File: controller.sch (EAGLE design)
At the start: 13 parts, among them IC1 7805DT, J1 POWER_JACKSLT, Q1 MOSFET-NCHANNELBSS123LT1G, Q2 MOSFET-PCHANNELSMD

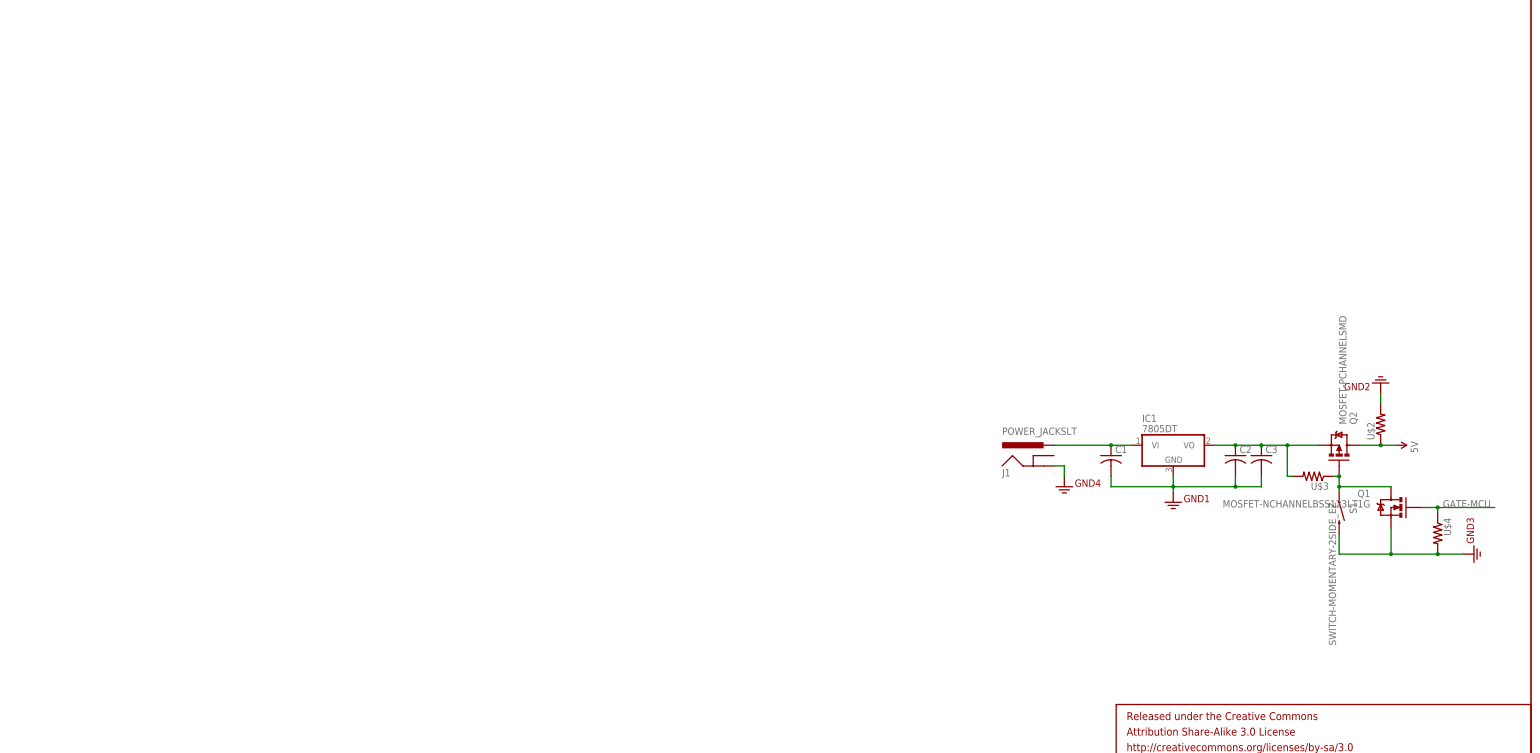
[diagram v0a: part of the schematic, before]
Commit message: removed parts order from repo
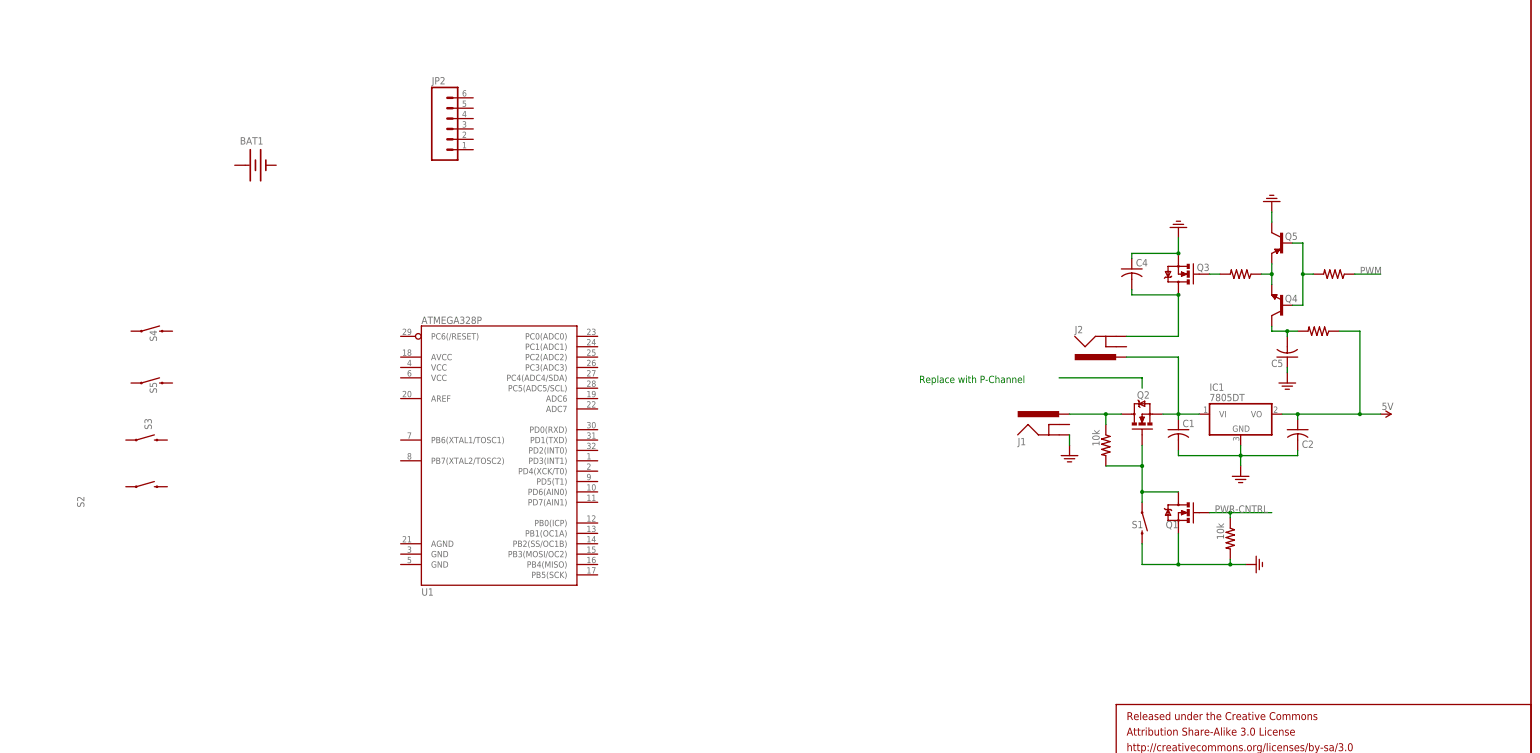
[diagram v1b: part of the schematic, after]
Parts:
- removed C3: (no value), adafruit:C-USC0805
- removed U$2: (no value), jt_parts:RESISTOR
- added BAT1: (no value), SparkFun-Electromechanical:BATTERY12PTH
- added C4, C5: (no value), adafruit:C-USC0805
- added J2: POWER_JACKSLT, SparkFun-Connectors:POWER_JACKSLT
- added JP2: (no value), SparkFun-Connectors:M06SIP
- added Q3: MOSFET-NCHANNELFDD8780, SparkFun-DiscreteSemi:MOSFET-NCHANNELFDD8780
- added Q4: (no value), SparkFun-DiscreteSemi:TRANSISTOR_NPNSOT23
- added Q5: MMBT4403, SparkFun-DiscreteSemi:TRANSISTOR_PNPMMBT4403
- added S2, S3, S4, S5: SWITCH-MOMENTARY-2SIDE_EZ, SparkFun-Electromechanical:SWITCH-MOMENTARY-2SIDE_EZ
- added U$5, U$6, U$7: (no value), jt_parts:RESISTOR
- added U1: ATMEGA328P, SparkFun-DigitalIC:ATMEGA328_SMT
- Q2: value MOSFET-PCHANNELSMD -> MOSFET-NCHANNELFDD8780; device SparkFun-DiscreteSemi:MOSFET-PCHANNELSMD -> SparkFun-DiscreteSemi:MOSFET-NCHANNELFDD8780
- U$3, U$4: value (none) -> 10k
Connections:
- net GATE-MCU renamed PWR-CNTRL
- removed net N$1: C2.1, C3.1, IC1.VO, Q2.S, U$3.2
- new net 12V-IN: J1.PWR, Q2.D, U$3.1
- new net N$10: Q1.D, Q2.G, S1.1, U$3.2
- new net N$3: Q3.G, U$5.2
- new net N$4: C4.2, J2.GND, Q3.D
- new net N$5: Q4.E, Q5.E, U$5.1
- new net NONE: Q4.B, Q5.B, U$6.2
- new net PWM: U$6.1
- net 12V: now also J2.PWR, Q2.S; no longer J1.PWR
- net 5V: now also C2.1, IC1.VO, U$7.1; no longer Q2.D, U$2.1
- net GND: now also C4.1, C5.1, Q3.S, Q5.C; no longer C3.2, U$2.2
- net N$2: now also C5.2, Q4.C, U$7.2; no longer Q1.D, Q2.G, S1.1, U$3.1
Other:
- note added: "Replace with P-Channel"
- moved on the sheet: C1, C2, IC1, J1, Q1, Q2, S1

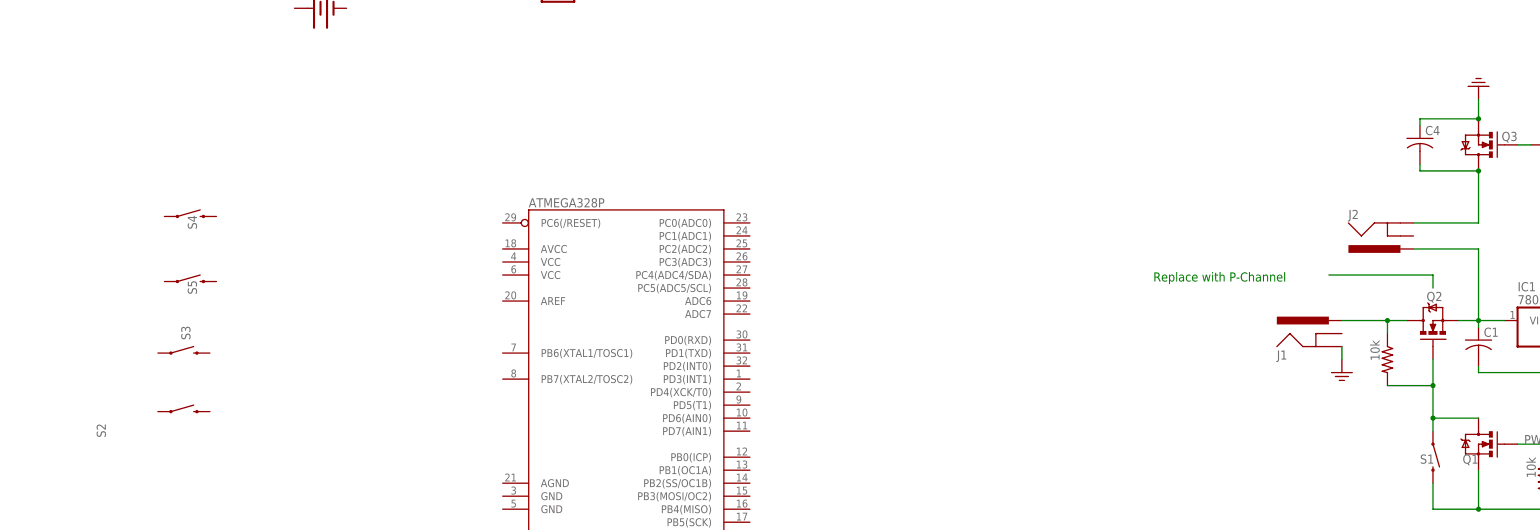
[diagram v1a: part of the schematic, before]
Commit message: reoriented controller to match with display.
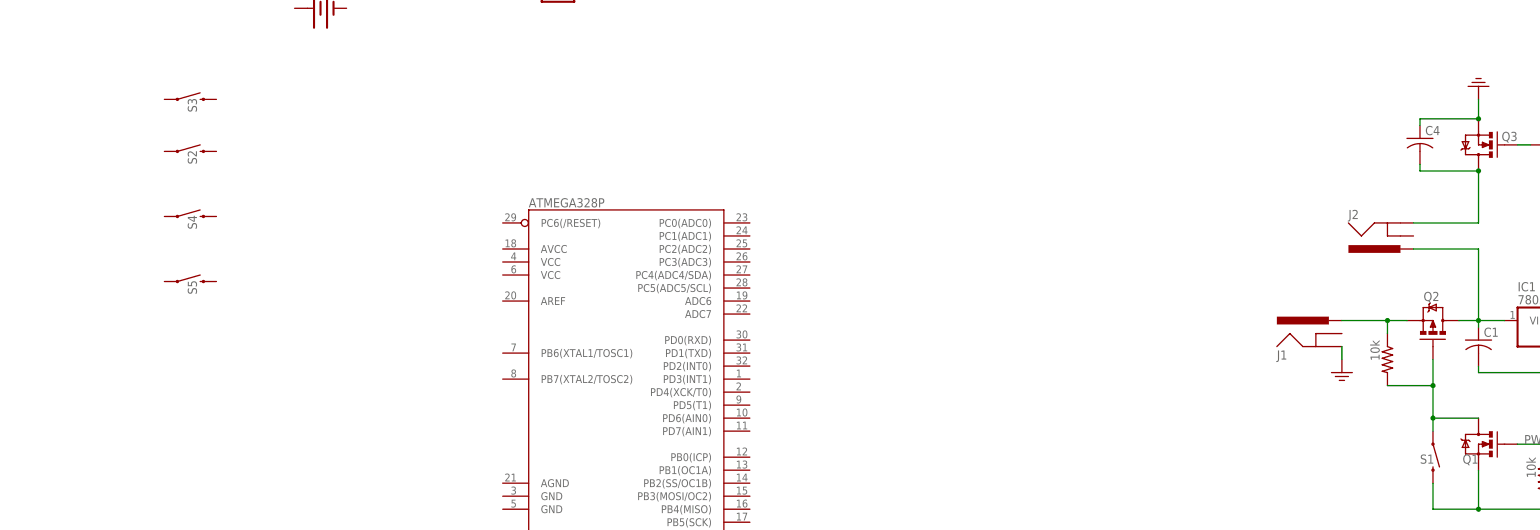
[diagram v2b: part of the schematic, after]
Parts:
- Q2: value MOSFET-NCHANNELFDD8780 -> MOSFET-PCHANNEL; device SparkFun-DiscreteSemi:MOSFET-NCHANNELFDD8780 -> SparkFun-DiscreteSemi:MOSFET-PCHANNEL
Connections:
- net N$4 renamed 12V-RETURN
- net 12V: now also Q2.D; no longer Q2.S
- net 12V-IN: now also Q2.S; no longer Q2.D
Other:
- note removed: "Replace with P-Channel"
- moved on the sheet: S2, S3
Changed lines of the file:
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@@
 <part name="GND5" library="SparkFun-Aesthetics" deviceset="GND2" device=""/>
 <part name="GND6" library="SparkFun-Aesthetics" deviceset="GND2" device=""/>
-<part name="Q2" library="SparkFun-DiscreteSemi" deviceset="MOSFET-NCHANNEL" device="FDD8780"/>
+<part name="Q2" library="SparkFun-DiscreteSemi" deviceset="MOSFET-PCHANNEL" device=""/>
 <part name="U$4" library="jt_parts" deviceset="RESISTOR" device="" value="10k"/>
 <part name="U$6" library="jt_parts" deviceset="RESISTOR" device=""/>
@@
 <part name="BAT1" library="SparkFun-Electromechanical" deviceset="BATTERY" device="12PTH"/>
 <part name="U1" library="SparkFun-DigitalIC" deviceset="ATMEGA328_SMT" device="" value="ATMEGA328P"/>
-<part name="S2" library="SparkFun-Electromechanical" deviceset="SWITCH-MOMENTARY-2" device="SIDE_EZ"/>
-<part name="S3" library="SparkFun-Electromechanical" deviceset="SWITCH-MOMENTARY-2" device="SIDE_EZ"/>
 <part name="S4" library="SparkFun-Electromechanical" deviceset="SWITCH-MOMENTARY-2" device="SIDE_EZ"/>
 <part name="S5" library="SparkFun-Electromechanical" deviceset="SWITCH-MOMENTARY-2" device="SIDE_EZ"/>
 <part name="JP2" library="SparkFun-Connectors" deviceset="M06" device="SIP"/>
+<part name="S2" library="SparkFun-Electromechanical" deviceset="SWITCH-MOMENTARY-2" device="SIDE_EZ"/>
+<part name="S3" library="SparkFun-Electromechanical" deviceset="SWITCH-MOMENTARY-2" device="SIDE_EZ"/>
 </parts>
 <sheets>
 <sheet>
 <plain>
-<text x="274.32" y="124.46" size="1.778" layer="91">Replace with P-Channel</text>
 </plain>
 <instances>
@@
 <instance part="GND5" gate="G$1" x="337.82" y="162.56" smashed="yes" rot="R180"/>
 <instance part="GND6" gate="G$1" x="360.68" y="168.91" smashed="yes" rot="R180"/>
-<instance part="Q2" gate="G$1" x="328.93" y="116.84" smashed="yes" rot="R90">
-<attribute name="NAME" x="327.66" y="120.65" size="1.778" layer="95"/>
+<instance part="Q2" gate="G$1" x="328.93" y="116.84" smashed="yes" rot="MR90">
+<attribute name="NAME" x="330.2" y="120.65" size="1.778" layer="95" rot="MR0"/>
 </instance>
 <instance part="U$4" gate="G$1" x="350.52" y="86.36" smashed="yes" rot="R270">
@@
 <instance part="BAT1" gate="G$1" x="111.76" y="177.8"/>
 <instance part="U1" gate="G$1" x="170.18" y="110.49"/>
-<instance part="S2" gate="G$1" x="85.09" y="99.06" smashed="yes">
-<attribute name="NAME" x="69.85" y="93.98" size="1.778" layer="95" rot="R90"/>
-</instance>
-<instance part="S3" gate="G$1" x="85.09" y="110.49" smashed="yes">
-<attribute name="NAME" x="86.36" y="113.03" size="1.778" layer="95" rot="R90"/>
-</instance>
 <instance part="S4" gate="G$1" x="86.36" y="137.16" smashed="yes">
 <attribute name="NAME" x="87.63" y="134.62" size="1.778" layer="95" rot="R90"/>
@@
 </instance>
 <instance part="JP2" gate="G$1" x="160.02" y="186.69"/>
+<instance part="S2" gate="G$1" x="86.36" y="149.86" smashed="yes">
+<attribute name="NAME" x="87.63" y="147.32" size="1.778" layer="95" rot="R90"/>
+</instance>
+<instance part="S3" gate="G$1" x="86.36" y="160.02" smashed="yes">
+<attribute name="NAME" x="87.63" y="157.48" size="1.778" layer="95" rot="R90"/>
+</instance>
 </instances>
 <busses>
@@
 </segment>
 </net>
-<net name="N$4" class="1">
+<net name="12V-RETURN" class="1">
 <segment>
 <pinref part="J2" gate="G$1" pin="GND"/>
@@
 <net name="N$10" class="0">
 <segment>
-<wire x1="328.93" y1="109.22" x2="328.93" y2="104.14" width="0.1524" layer="91"/>
 <wire x1="328.93" y1="104.14" x2="320.04" y2="104.14" width="0.1524" layer="91"/>
 <pinref part="U$3" gate="G$1" pin="2"/>
@@
 <wire x1="337.82" y1="97.79" x2="328.93" y2="97.79" width="0.1524" layer="91"/>
 <wire x1="328.93" y1="104.14" x2="328.93" y2="97.79" width="0.1524" layer="91"/>
-<junction x="328.93" y="104.14"/>
 <junction x="328.93" y="97.79"/>
 <pinref part="Q2" gate="G$1" pin="G"/>
+<wire x1="328.93" y1="104.14" x2="328.93" y2="109.22" width="0.1524" layer="91"/>
+<junction x="328.93" y="104.14"/>
 </segment>
 </net>
@@
 <pinref part="J2" gate="G$1" pin="PWR"/>
 <wire x1="325.12" y1="130.81" x2="337.82" y2="130.81" width="0.1524" layer="91"/>
-<pinref part="Q2" gate="G$1" pin="S"/>
 <pinref part="IC1" gate="A1" pin="VI"/>
-<wire x1="334.01" y1="116.84" x2="337.82" y2="116.84" width="0.1524" layer="91"/>
 <pinref part="C1" gate="G$1" pin="1"/>
 <wire x1="337.82" y1="116.84" x2="342.9" y2="116.84" width="0.1524" layer="91"/>
@@
 <junction x="337.82" y="116.84"/>
 <wire x1="337.82" y1="130.81" x2="337.82" y2="116.84" width="0.1524" layer="91"/>
-</segment>
-</net>
-<net name="N$1" class="0">
-<segment>
-<wire x1="308.61" y1="125.73" x2="328.93" y2="125.73" width="0.1524" layer="91"/>
-<wire x1="328.93" y1="125.73" x2="328.93" y2="123.19" width="0.1524" layer="91"/>
+<pinref part="Q2" gate="G$1" pin="D"/>
+<wire x1="334.01" y1="116.84" x2="337.82" y2="116.84" width="0.1524" layer="91"/>
 </segment>
 </net>
@@
 <segment>
 <pinref part="J1" gate="G$1" pin="PWR"/>
-<pinref part="Q2" gate="G$1" pin="D"/>
 <wire x1="311.15" y1="116.84" x2="320.04" y2="116.84" width="0.1524" layer="91"/>
 <pinref part="U$3" gate="G$1" pin="1"/>
-<wire x1="320.04" y1="116.84" x2="323.85" y2="116.84" width="0.1524" layer="91"/>
 <wire x1="320.04" y1="114.3" x2="320.04" y2="116.84" width="0.1524" layer="91"/>
+<pinref part="Q2" gate="G$1" pin="S"/>
+<wire x1="323.85" y1="116.84" x2="320.04" y2="116.84" width="0.1524" layer="91"/>
 <junction x="320.04" y="116.84"/>
 </segment>

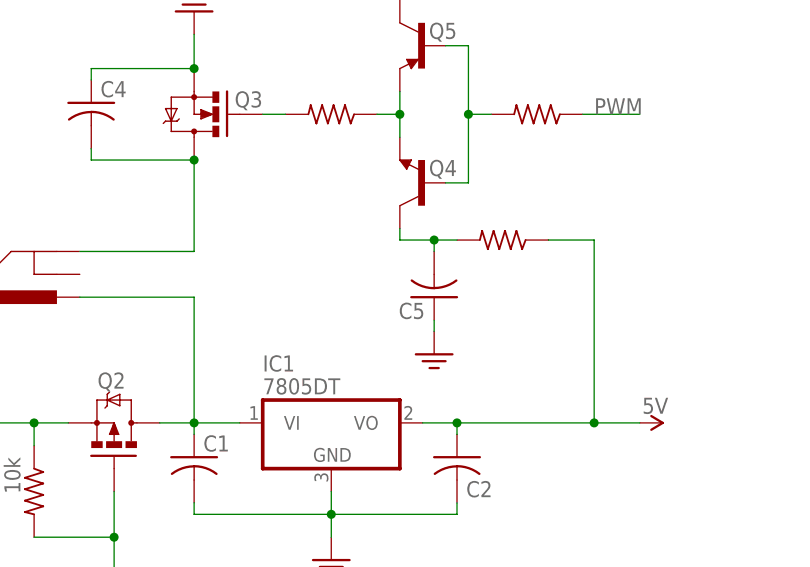
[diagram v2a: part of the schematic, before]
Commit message: fixed inconsistency between board and schematic.
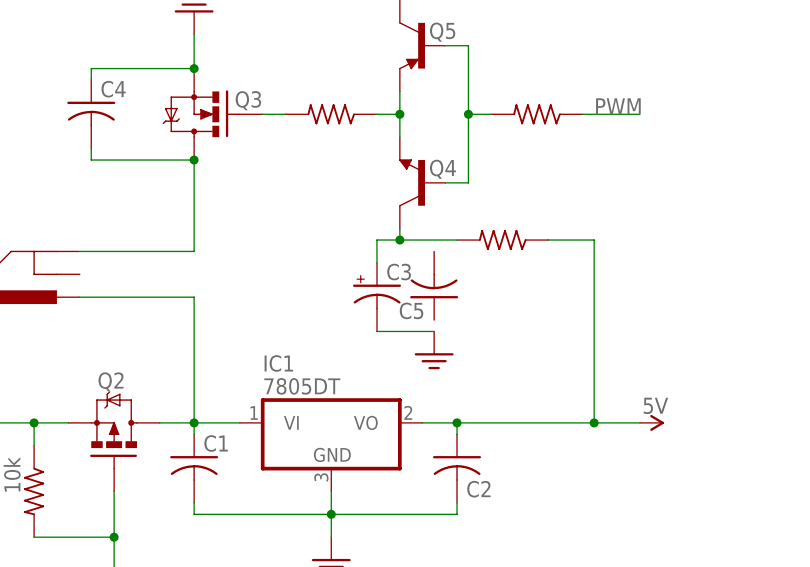
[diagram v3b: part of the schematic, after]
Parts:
- added C3: (no value), adafruit:CPOL-USE22-10AXIAL
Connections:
- new net 3.3V: C3.-
- net GND: no longer C5.1
- net N$2: now also C3.+; no longer C5.2
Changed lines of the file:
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@@
 <setting verticaltext="up"/>
 </settings>
-<grid distance="0.05" unitdist="inch" unit="inch" style="lines" multiple="1" display="yes" altdistance="0.01" altunitdist="inch" altunit="inch"/>
+<grid distance="0.05" unitdist="inch" unit="inch" style="lines" multiple="1" display="no" altdistance="0.01" altunitdist="inch" altunit="inch"/>
 <layers>
 <layer number="1" name="Top" color="4" fill="1" visible="no" active="no"/>
@@
 <part name="S2" library="SparkFun-Electromechanical" deviceset="SWITCH-MOMENTARY-2" device="SIDE_EZ"/>
 <part name="S3" library="SparkFun-Electromechanical" deviceset="SWITCH-MOMENTARY-2" device="SIDE_EZ"/>
+<part name="C3" library="adafruit" deviceset="CPOL-US" device="E22-10AXIAL"/>
 </parts>
 <sheets>
@@
 <attribute name="NAME" x="87.63" y="157.48" size="1.778" layer="95" rot="R90"/>
 </instance>
+<instance part="C3" gate="G$1" x="358.14" y="132.08"/>
 </instances>
 <busses>
@@
 <wire x1="360.68" y1="166.37" x2="360.68" y2="163.83" width="0.1524" layer="91"/>
 </segment>
-<segment>
-<pinref part="C5" gate="G$1" pin="1"/>
-<pinref part="GND7" gate="G$1" pin="3.3V"/>
-<wire x1="364.49" y1="128.27" x2="364.49" y2="127" width="0.1524" layer="91"/>
-</segment>
 </net>
 <net name="RCK" class="0">
@@
 <pinref part="Q4" gate="G$1" pin="C"/>
 <wire x1="360.68" y1="138.43" x2="360.68" y2="137.16" width="0.1524" layer="91"/>
-<wire x1="360.68" y1="137.16" x2="364.49" y2="137.16" width="0.1524" layer="91"/>
-<pinref part="C5" gate="G$1" pin="2"/>
-<wire x1="364.49" y1="137.16" x2="364.49" y2="135.89" width="0.1524" layer="91"/>
+<wire x1="360.68" y1="137.16" x2="367.03" y2="137.16" width="0.1524" layer="91"/>
 <pinref part="U$7" gate="G$1" pin="2"/>
-<wire x1="364.49" y1="137.16" x2="367.03" y2="137.16" width="0.1524" layer="91"/>
-<junction x="364.49" y="137.16"/>
+<wire x1="360.68" y1="137.16" x2="358.14" y2="137.16" width="0.1524" layer="91"/>
+<junction x="360.68" y="137.16"/>
+<pinref part="C3" gate="G$1" pin="+"/>
+<wire x1="358.14" y1="134.62" x2="358.14" y2="137.16" width="0.1524" layer="91"/>
 </segment>
 </net>
@@
 </segment>
 </net>
+<net name="3.3V" class="0">
+<segment>
+<pinref part="GND7" gate="G$1" pin="3.3V"/>
+<pinref part="C3" gate="G$1" pin="-"/>
+<wire x1="364.49" y1="127" x2="358.14" y2="127" width="0.1524" layer="91"/>
+</segment>
+</net>
